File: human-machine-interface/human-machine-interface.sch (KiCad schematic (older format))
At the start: 20 parts, among them J1 USB_B_Micro, J2 Conn_01x04_Male, J3 Conn_01x04_Male, J4 Conn_01x04_Male, SW1 SW_DPDT_x2, SW2 SW_Push, SW3 SW_Push, U1 Teensy3.2, U2 NRF24L01+

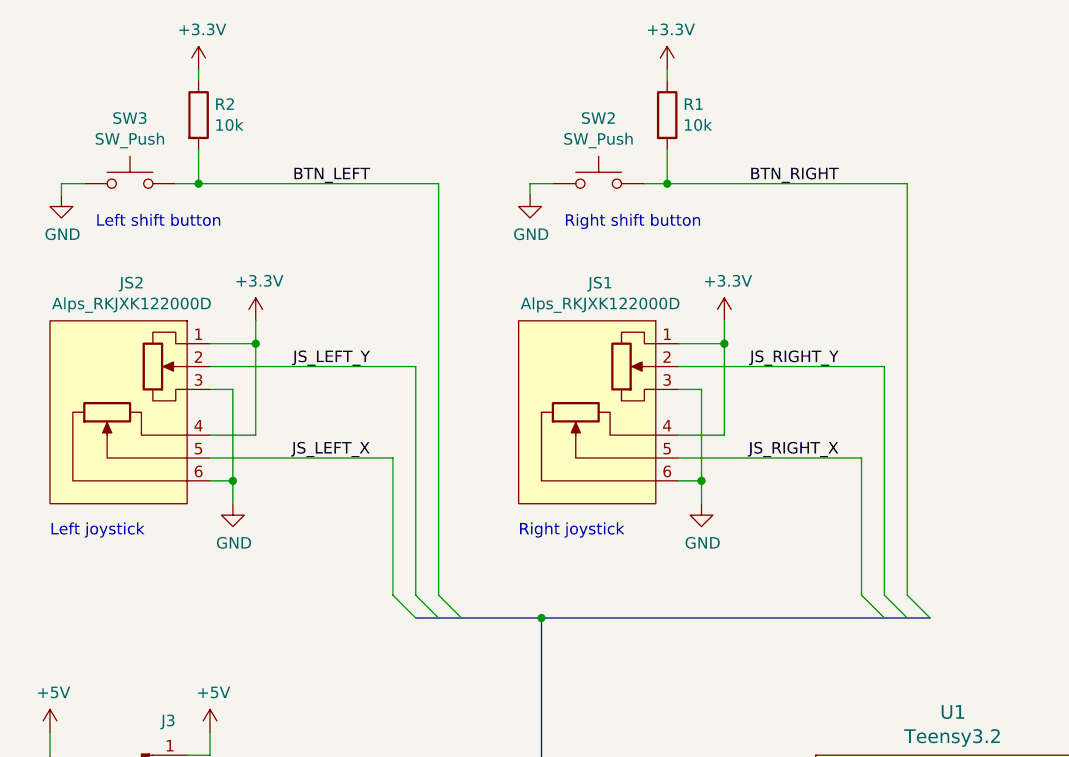
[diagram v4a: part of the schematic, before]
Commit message: Move the HMI's thumbsticks to separate boards
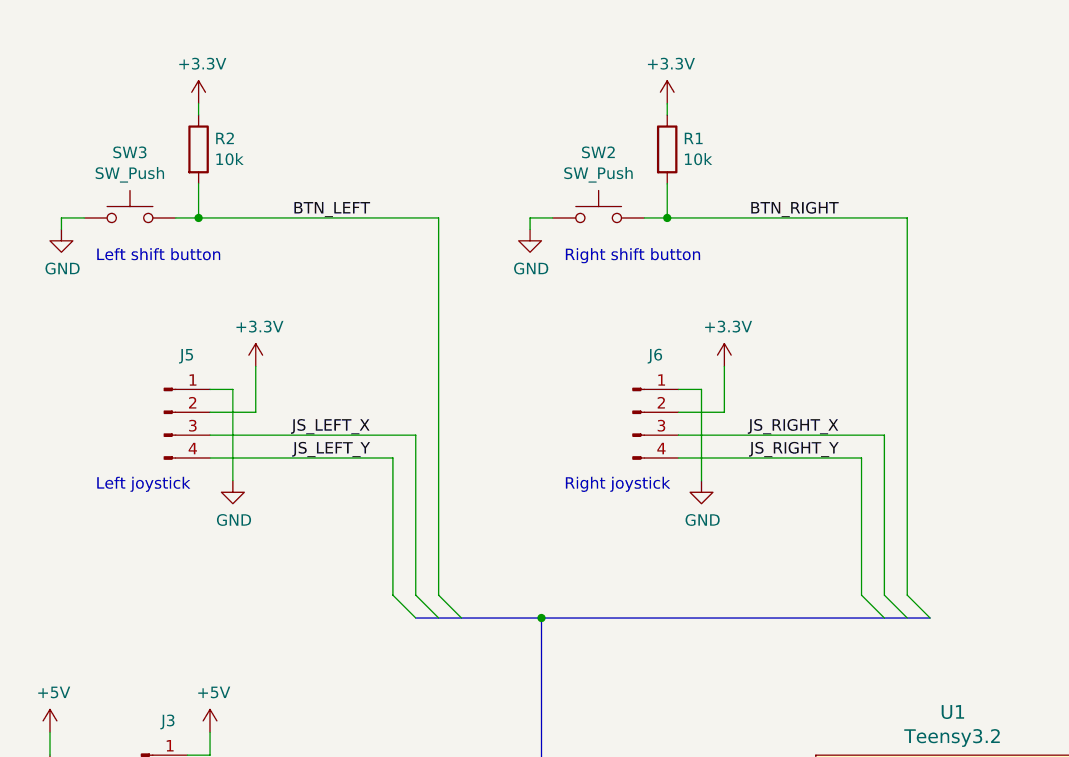
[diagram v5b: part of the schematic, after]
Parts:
- removed JS1, JS2: Alps_RKJXK122000D, earth-rover-custom-footprints:Alps_RKJXK122000D, symbol earth-rover-custom-symbols:Alps_RKJXK122000D
- added J5, J6: Conn_01x04_Male, symbol Connector:Conn_01x04_Male
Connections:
- net +3V3: now also J5.2 (Pin_2), J6.2 (Pin_2)
- net GND: now also J5.1 (Pin_1), J6.1 (Pin_1)
- net JS_LEFT_X: now also J5.3 (Pin_3)
- net JS_LEFT_Y: now also J5.4 (Pin_4)
- net JS_RIGHT_X: now also J6.3 (Pin_3)
- net JS_RIGHT_Y: now also J6.4 (Pin_4)
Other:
- moved on the sheet: R1, R2, SW2, SW3

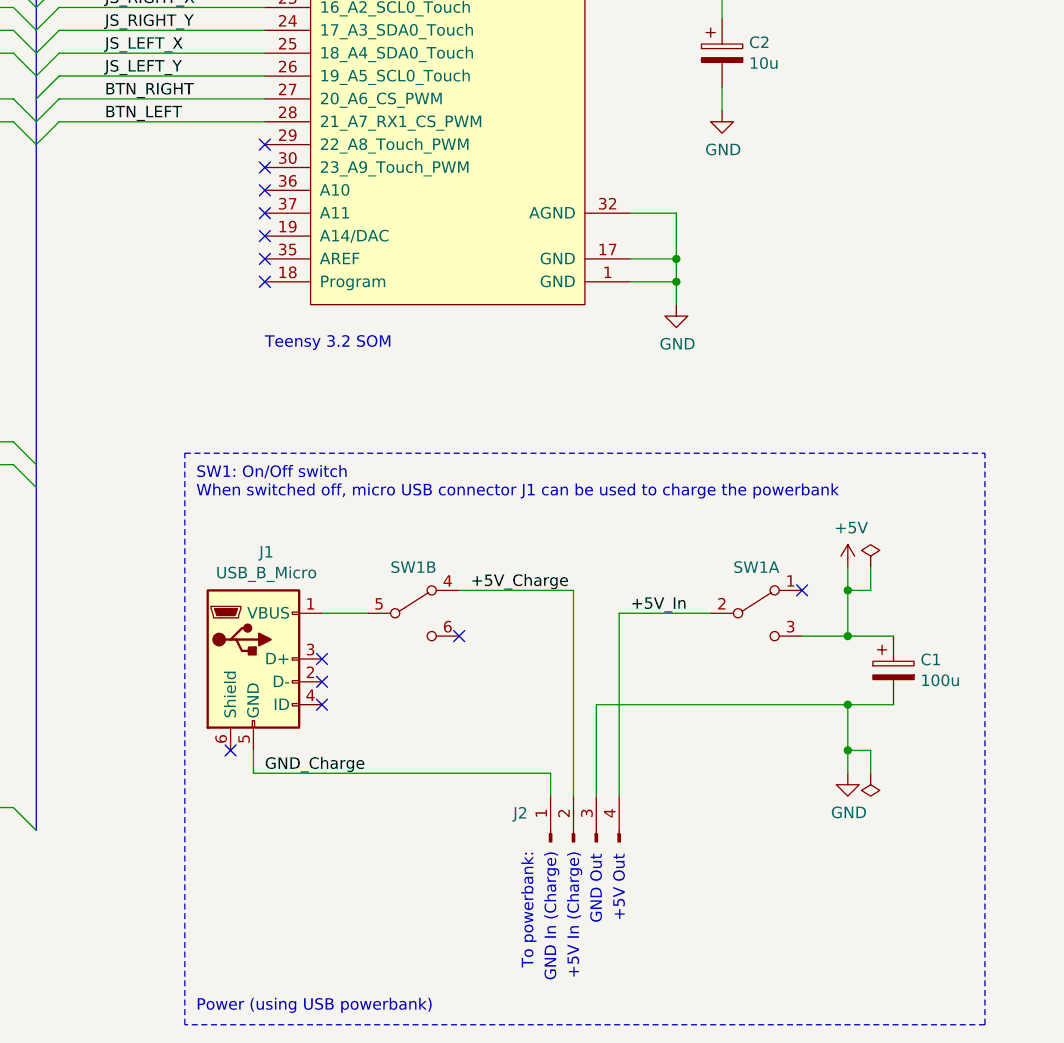
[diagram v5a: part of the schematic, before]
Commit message: Update power supply of HMI
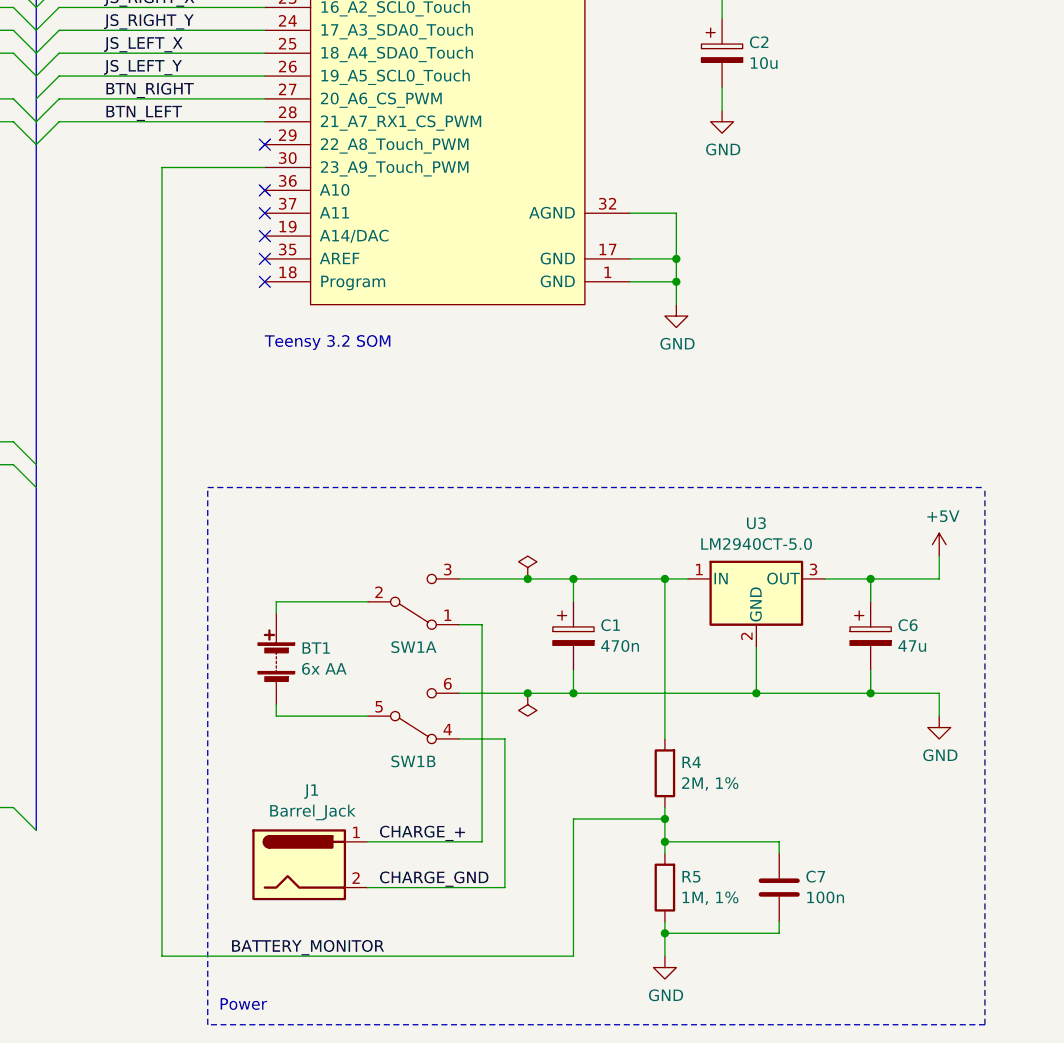
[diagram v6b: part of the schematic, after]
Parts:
- removed J1: USB_B_Micro, symbol Connector:USB_B_Micro
- removed J2: Conn_01x04_Male, symbol Connector:Conn_01x04_Male
- added BT1: 6x AA, symbol Device:Battery
- added C6: 47u, symbol Device:CP
- added C7: 100n, symbol Device:C
- added J1: Barrel_Jack, symbol Connector:Barrel_Jack
- added R4: 2M, 1%, symbol Device:R
- added R5: 1M, 1%, symbol Device:R
- added U3: LM2940CT-5.0, Package_TO_SOT_THT:TO-220-3_Vertical, symbol earth-rover-custom-symbols:LM2940CT-5.0
- C1: value 100u -> 470n
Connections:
- net +5V: now also C6.1, U3.3 (OUT); no longer C1.1, SW1.3 (C)
- net GND: now also SW1.6 (C), C6.2, C7.2, R5.1, U3.2 (GND)
- net at SW1.5 (B): now also BT1.2 (-)
- net CHARGE_+: now reaches SW1.1 (A)
- net CHARGE_+: now also J1.1
- net BATTERY_MONITOR: now reaches U1.30 (23_A9_Touch_PWM)
- net BATTERY_MONITOR: now also C7.1, R4.1, R5.2
- net +5V_Charge renamed CHARGE_GND
- net CHARGE_GND: now also J1.2
- net +5V_In: no longer names the net of SW1.2 (B)
- net +5V_In: now also BT1.1 (+)
- new net: C1.1, R4.2, SW1.3 (C), U3.1 (IN)
- no-connect marks 20 -> 13
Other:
- note added: "Power"
- note removed: "+5V In (Charge)"
- note removed: "+5V Out"
- note removed: "GND In (Charge)"
- note removed: "GND Out"
- note removed: "Power (using USB powerbank)"
- note removed: "SW1: On/Off switch\nWhen switched off, micro USB connector J1 can be used to charge the powerbank"
- note removed: "To powerbank:"
- moved on the sheet: SW1A, SW1B

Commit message: Review schematics
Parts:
- BT1: value 6x AA -> 6x NiMH AA
- J5: renamed from J1; value Barrel_Jack -> 5.4mm/2.5mm
- renumbered C4 to C1, C3 to C2, C5 to C3, C1 to C4, C2 to C5, C7 to C6, C6 to C7, J3 to J1, J4 to J2, J5 to J3, J6 to J4, R2 to R1, R3 to R2, R1 to R3, SW3 to SW1, SW1 to SW3, U2 to U1, U1 to U2
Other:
- moved on the sheet: BT1, J5

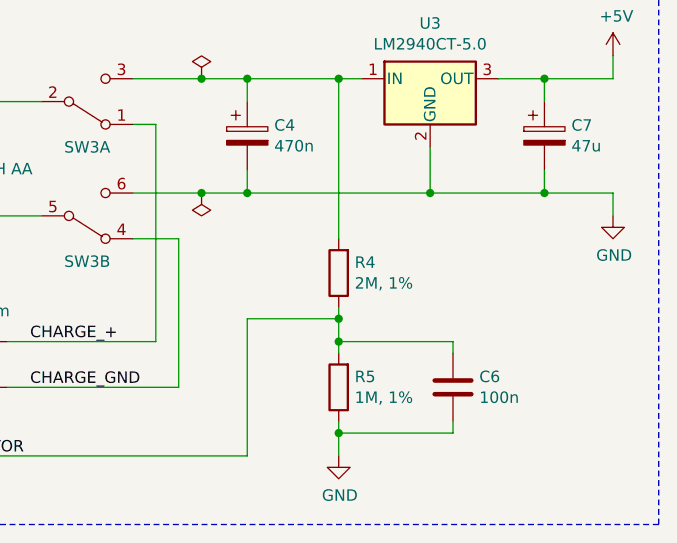
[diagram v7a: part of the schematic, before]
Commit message: Correct resistor value for battery monitor
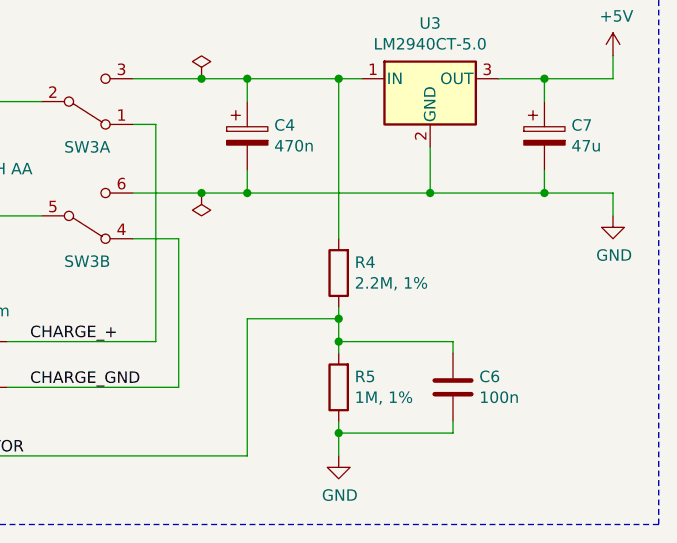
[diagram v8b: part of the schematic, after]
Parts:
- R4: value 2M, 1% -> 2.2M, 1%
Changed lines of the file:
@@
 Sheet 1 1
 Title "Earth Rover"
-Date "2019-12-20"
-Rev "6"
+Date "2019-12-21"
+Rev "7"
 Comp "Vijfendertig BVBA"
 Comment1 "Maarten De Munck"
@@
 P 6250 8950
 F 0 "R4" H 6180 8904 50  0000 R CNN
-F 1 "2M, 1%" H 6180 8995 50  0000 R CNN
+F 1 "2.2M, 1%" H 6180 8995 50  0000 R CNN
 F 2 "" V 6180 8950 50  0001 C CNN
 F 3 "~" H 6250 8950 50  0001 C CNN
